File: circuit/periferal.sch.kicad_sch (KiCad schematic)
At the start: 51 parts, among them J3 SH_01x04, J4 SH_01x04, J5 SH_01x03, J6 SH_01x03, J7 Conn_02x05, Q4 DMN1054UCB4, Q5 DMN1054UCB4, Q6 DMN1054UCB4, Q7 DMN1054UCB4, Q8 DMN1054UCB4, U7 BMI088

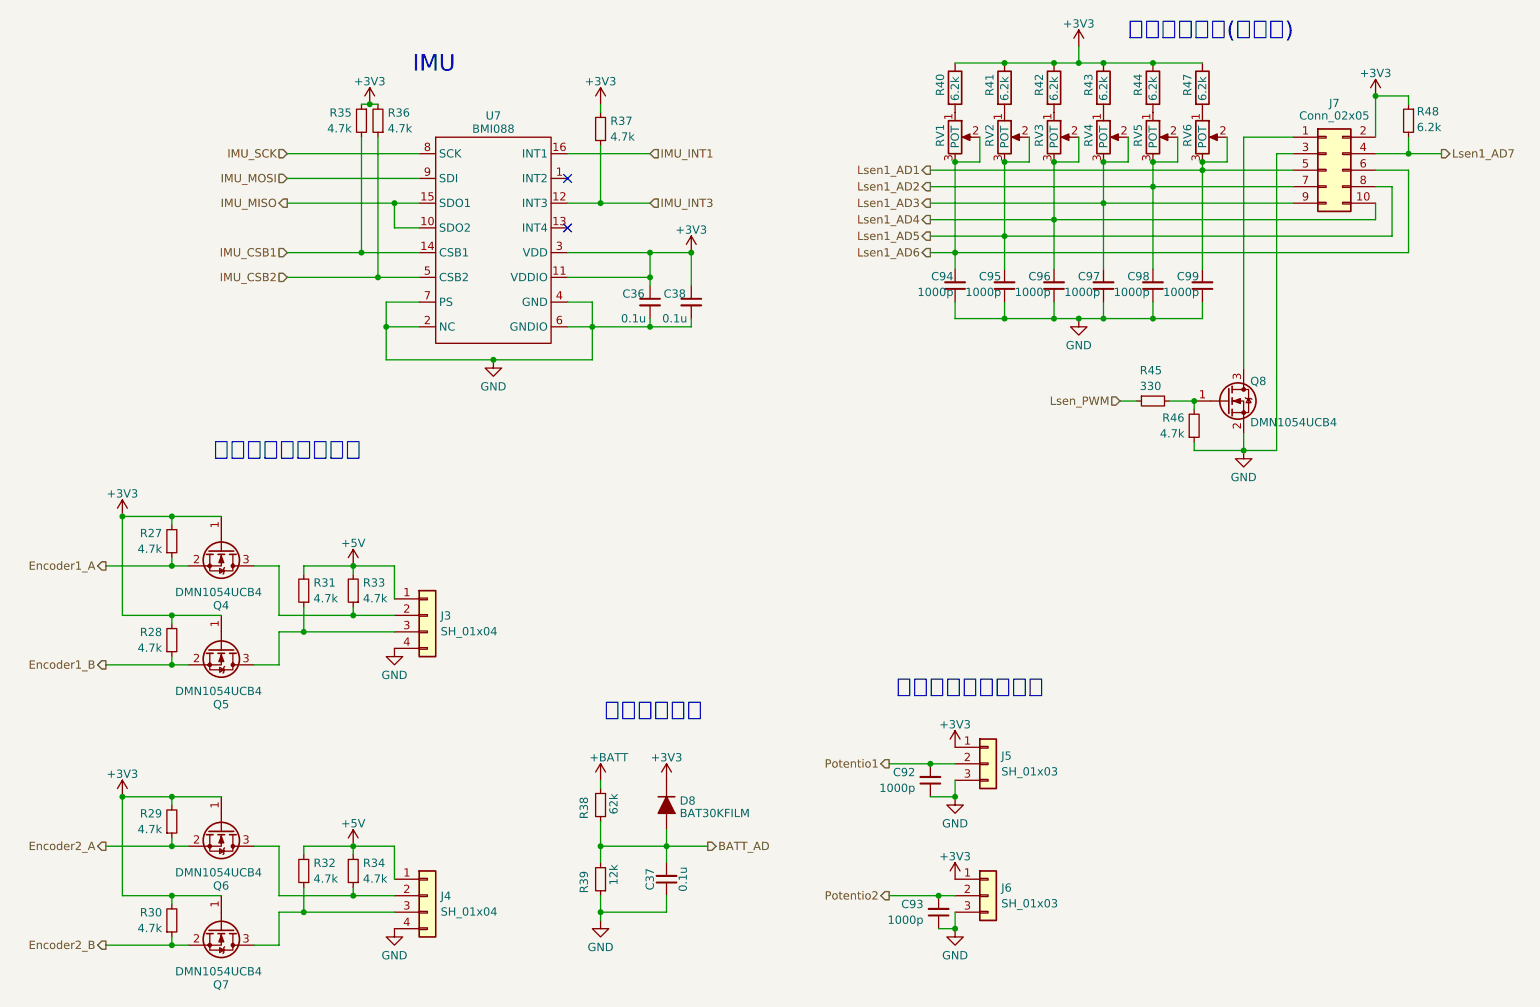
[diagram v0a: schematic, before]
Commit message: スマコンの設定変更 回路図変更
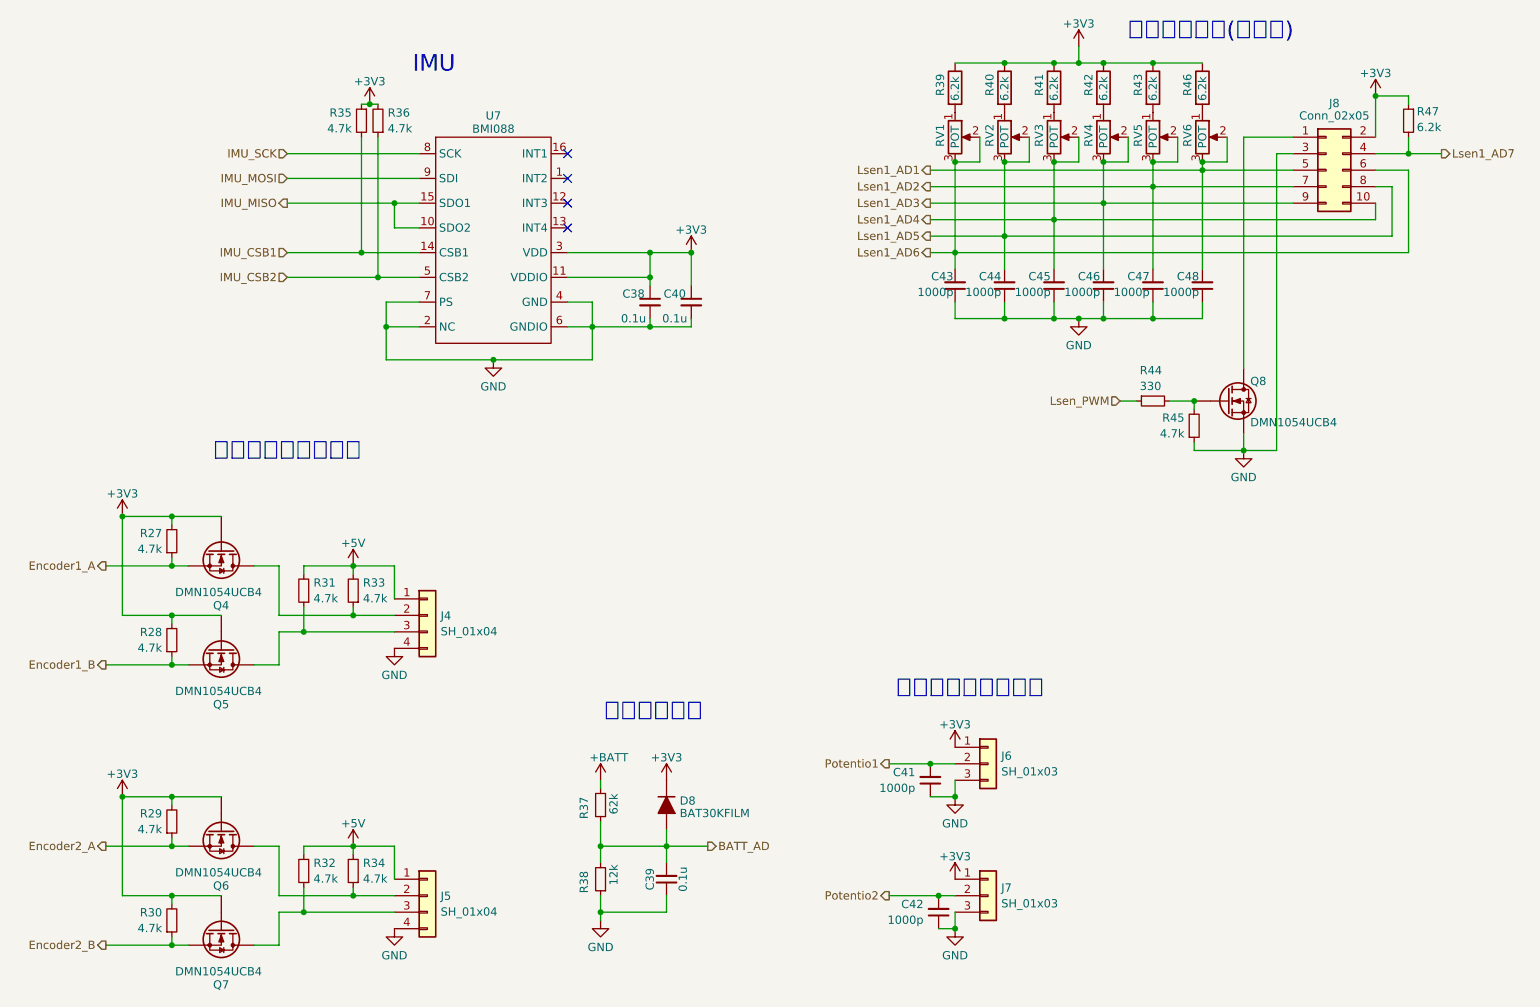
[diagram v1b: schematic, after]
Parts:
- removed R37: 4.7k, Resistor_SMD:R_0402_1005Metric, symbol Device:R_Small
- Q4, Q5, Q6, Q7, Q8: symbol Device:Q_NMOS_GSD -> Device:Q_NMOS
- U7: symbol robocon:BMI088 -> robot_contest:BMI088
- renumbered C36 to C38, C37 to C39, C38 to C40, C92 to C41, C93 to C42, C94 to C43, C95 to C44, C96 to C45, C97 to C46, C98 to C47, C99 to C48, J3 to J4, J4 to J5, J5 to J6, J6 to J7, J7 to J8, R38 to R37, R39 to R38, R40 to R39, R41 to R40, R42 to R41, R43 to R42, R44 to R43, R45 to R44, R46 to R45, R47 to R46, R48 to R47
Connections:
- net +3V3: now also Q4.G, Q5.G, Q6.G, Q7.G; no longer Q4.1 (G), Q5.1 (G), Q6.1 (G), Q7.1 (G)
- net Encoder1_A: now also Q4.S; no longer Q4.2 (S)
- net Encoder1_B: now also Q5.S; no longer Q5.2 (S)
- net Encoder2_A: now also Q6.S; no longer Q6.2 (S)
- net Encoder2_B: now also Q7.S; no longer Q7.2 (S)
- net GND: now also Q8.S; no longer Q8.2 (S)
- net at J4.3 (Pin_3), R31.1: now also Q5.D; no longer Q5.3 (D)
- net at J5.2 (Pin_2), R34.1: now also Q6.D; no longer Q6.3 (D)
- net at R44.2, R45.2: now also Q8.G; no longer Q8.1 (G)
- net at J5.3 (Pin_3), R32.1: now also Q7.D; no longer Q7.3 (D)
- net at J8.1 (Pin_1): now also Q8.D; no longer Q8.3 (D)
- net at J4.2 (Pin_2), R33.1: now also Q4.D; no longer Q4.3 (D)
- net IMU_INT1: no longer names the net of U7.16 (INT1)
- net IMU_INT3: no longer names the net of U7.12 (INT3)
- no-connect marks 2 -> 4
